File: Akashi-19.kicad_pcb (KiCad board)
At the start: 2 copper layers, 121.9 x 95.2 mm, 7 parts, among them J1 GROVE I2C, J2 Conn_01x20_Socket, J3 Conn_01x20_Socket, J4 QWIIC, J5 SERIAL, SW1 RESET, U1 Pico

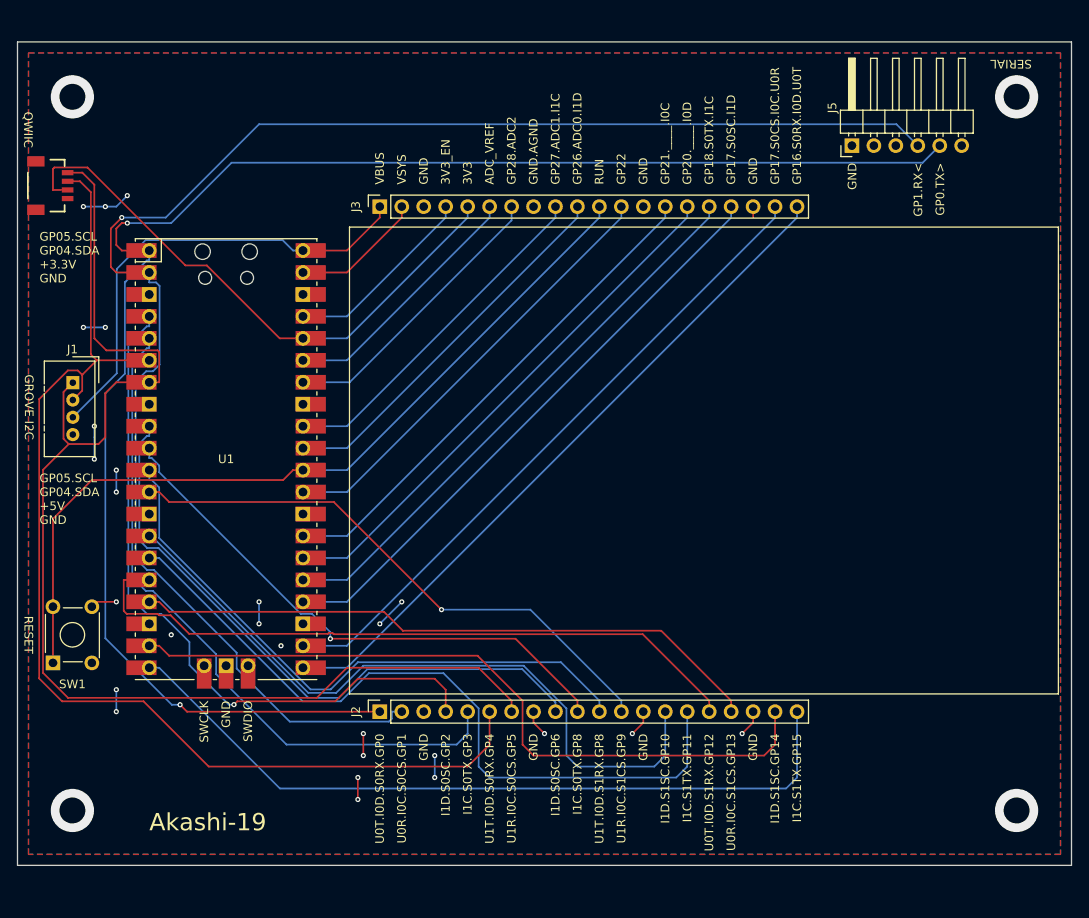
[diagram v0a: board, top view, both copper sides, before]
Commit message: Part position updated.
Wire is more beautiful.
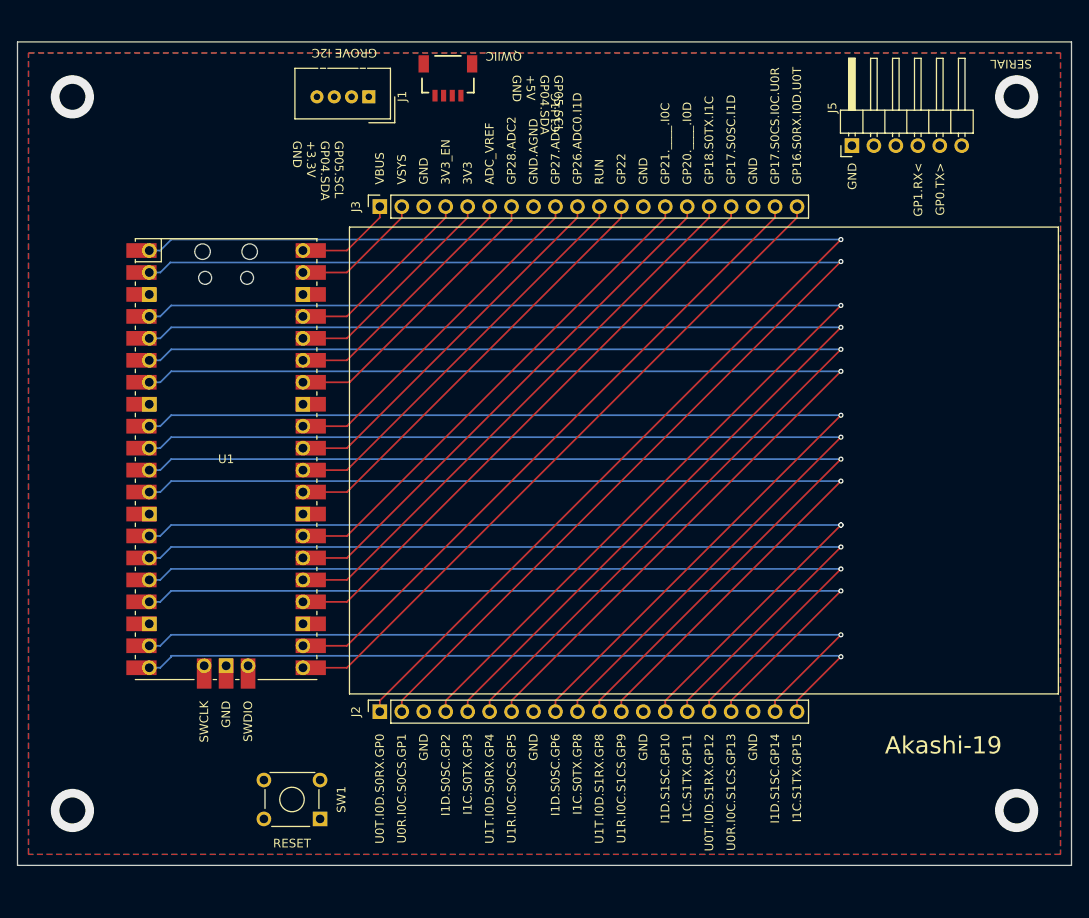
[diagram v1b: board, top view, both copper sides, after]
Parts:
- moved J1 47.6 mm to (128.3, 58.4), turned to -90 degrees
- moved J4 45.2 mm to (137.4, 58.3), turned to 180 degrees
- moved SW1 35.8 mm to (122.6, 141.9), turned to 180 degrees
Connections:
- J4 pad NC1: unconnected-(J4-NC-PadNC1) -> GND
- J4 pad NC2: unconnected-(J4-NC-PadNC2) -> GND
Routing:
- net Net-(J2-Pin_4): track 81.3 -> 146.5 mm
- net Net-(J2-Pin_5): track 79.9 -> 142.9 mm, vias 0 -> 1
- net Net-(J2-Pin_10): track 64.5 -> 124.9 mm
- net Net-(J2-Pin_9): track 73.6 -> 128.5 mm, vias 0 -> 1
- net Net-(J2-Pin_12): track 65.9 -> 117.7 mm
- net Net-(J2-Pin_11): track 71.1 -> 121.3 mm, vias 0 -> 1
- net Net-(J3-Pin_11): track 95.6 -> 47.7 mm
- net GND: track 44.3 -> 0.00 mm, vias 31 -> 4
- net +5V: track 54.4 -> 11.7 mm
- net +3.3V: track 66.7 -> 26.1 mm
- net /RX: track 184.8 -> 153.6 mm
- net /TX: track 187.7 -> 157.2 mm, vias 2 -> 1
- net Net-(J2-Pin_14): track 82.1 -> 110.5 mm, vias 0 -> 2
- net Net-(J2-Pin_17): track 73.3 -> 99.8 mm, vias 0 -> 1
- net Net-(J2-Pin_16): track 79.9 -> 103.4 mm, vias 0 -> 1
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
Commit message: Board resized.
111.7mm length.
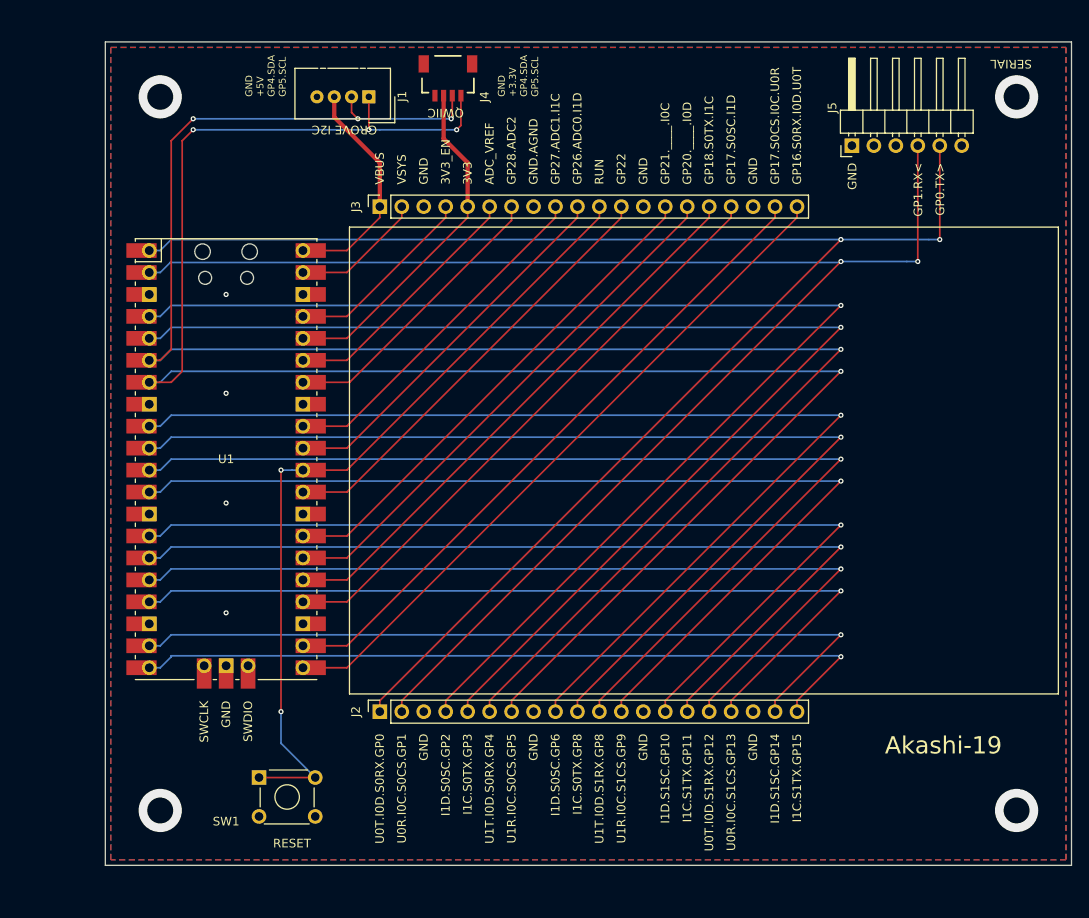
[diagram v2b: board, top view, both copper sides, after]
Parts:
- moved SW1 8.53 mm to (115.6, 137.2), turned to 0 degrees
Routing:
- net /SCL: track 135.7 -> 206.9 mm, vias 1 -> 4
- net /SDA: track 139.3 -> 205.4 mm, vias 1 -> 4
- net Net-(J3-Pin_11): track 47.7 -> 93.9 mm, vias 0 -> 2
- net /TX: track 157.2 -> 179.5 mm, vias 1 -> 2
- net /RX: track 153.6 -> 175.9 mm, vias 1 -> 2
- net +5V: track 11.7 -> 26.6 mm
- net +3.3V: track 26.1 -> 40.1 mm
- net Net-(J2-Pin_14): vias 2 -> 1
- net GND: vias 4 -> 8
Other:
- board size 121.9 x 95.2 mm -> 111.8 x 95.2 mm
- board text added: "GND +3.3V GP4.SDA GP5.SCL"
- board text added: "GND +5V GP4.SDA GP5.SCL"
- board text removed: "GP05.SCL GP04.SDA +3.3V GND"
- board text removed: "GP05.SCL GP04.SDA +5V GND"

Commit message: Change pin names font to NOTO SANS MONO
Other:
- board text added: "GND 3V3 GP4.SDA GP5.SCL"
- board text added: "GND VBUS GP4.SDA GP5.SCL"
- board text added: "U0T I0D S0RX GP0"
- board text removed: "GND +3.3V GP4.SDA GP5.SCL"
- board text removed: "GND +5V GP4.SDA GP5.SCL"
- board text removed: "U0T.I0D.S0RX.GP0"

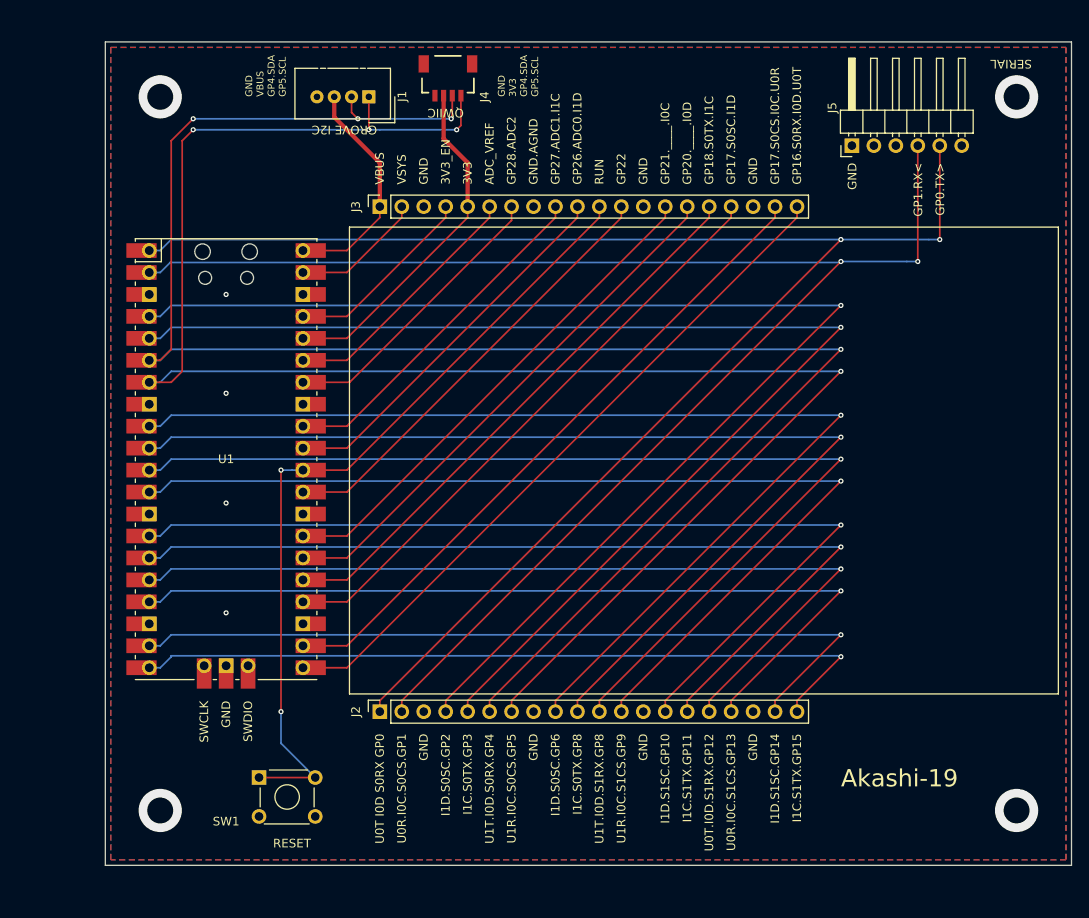
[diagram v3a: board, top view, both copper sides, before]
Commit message: Pin name description is updated.
- Separated by ' '.
- Grove and Qwiik description by table.
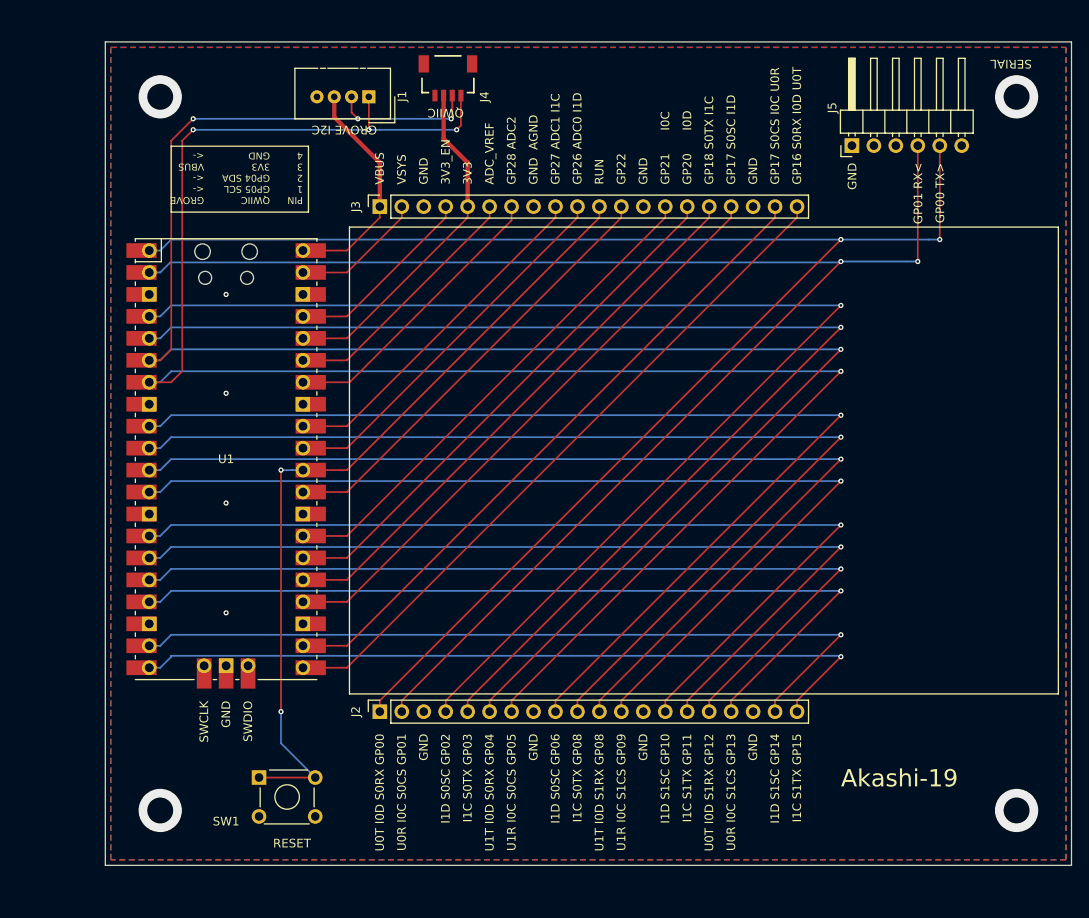
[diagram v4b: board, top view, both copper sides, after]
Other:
- board text added: "GND AGND"
- board text added: "GP00 TX>"
- board text added: "GP01 RX<"
- board text added: "GP16 S0RX I0D U0T"
- board text added: "GP17 S0CS I0C U0R"
- board text added: "GP17 S0SC I1D"
- board text added: "GP18 S0TX I1C"
- board text added: "GP20 I0D"
- board text added: "GP21 I0C"
- board text added: "GP26 ADC0 I1D"
- board text added: "GP27 ADC1 I1C"
- board text added: "GP28 ADC2"
- board text added: "GROVE <- <- VBUS <-"
- board text added: "I1C S0TX GP03"
- board text added: "I1C S0TX GP08"
- board text added: "I1C S1TX GP11"
- board text added: "I1C S1TX GP15"
- board text added: "I1D S0SC GP02"
- board text added: "I1D S0SC GP06"
- board text added: "I1D S1SC GP10"
- board text added: "I1D S1SC GP14"
- board text added: "PIN 1 2 3 4"
- board text added: "QWIIC GP05 SCL GP04 SDA 3V3 GND"
- board text added: "U0R I0C S0CS GP01"
- board text added: "U0R I0C S1CS GP13"
- board text added: "U0T I0D S0RX GP00"
- board text added: "U0T I0D S1RX GP12"
- board text added: "U1R I0C S0CS GP05"
- board text added: "U1R I0C S1CS GP09"
- board text added: "U1T I0D S0RX GP04"
- board text added: "U1T I0D S1RX GP08"
- board text removed: "GND 3V3 GP4.SDA GP5.SCL"
- board text removed: "GND VBUS GP4.SDA GP5.SCL"
- board text removed: "GND.AGND"
- board text removed: "GP0.TX>"
- board text removed: "GP1.RX<"
- board text removed: "GP16.S0RX.I0D.U0T"
- board text removed: "GP17.S0CS.I0C.U0R"
- board text removed: "GP17.S0SC.I1D"
- board text removed: "GP18.S0TX.I1C"
- board text removed: "GP20.____.I0D"
- board text removed: "GP21.____.I0C"
- board text removed: "GP26.ADC0.I1D"
- board text removed: "GP27.ADC1.I1C"
- board text removed: "GP28.ADC2"
- board text removed: "I1C.S0TX.GP3"
- board text removed: "I1C.S0TX.GP8"
- board text removed: "I1C.S1TX.GP11"
- board text removed: "I1C.S1TX.GP15"
- board text removed: "I1D.S0SC.GP2"
- board text removed: "I1D.S0SC.GP6"
- board text removed: "I1D.S1SC.GP10"
- board text removed: "I1D.S1SC.GP14"
- board text removed: "U0R.I0C.S0CS.GP1"
- board text removed: "U0R.I0C.S1CS.GP13"
- board text removed: "U0T I0D S0RX GP0"
- board text removed: "U0T.I0D.S1RX.GP12"
- board text removed: "U1R.I0C.S0CS.GP5"
- board text removed: "U1R.I0C.S1CS.GP9"
- board text removed: "U1T.I0D.S0RX.GP4"
- board text removed: "U1T.I0D.S1RX.GP8"

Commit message: The font of Signal name has been changed.
Now, Ubuntu Mono. 1.1mm
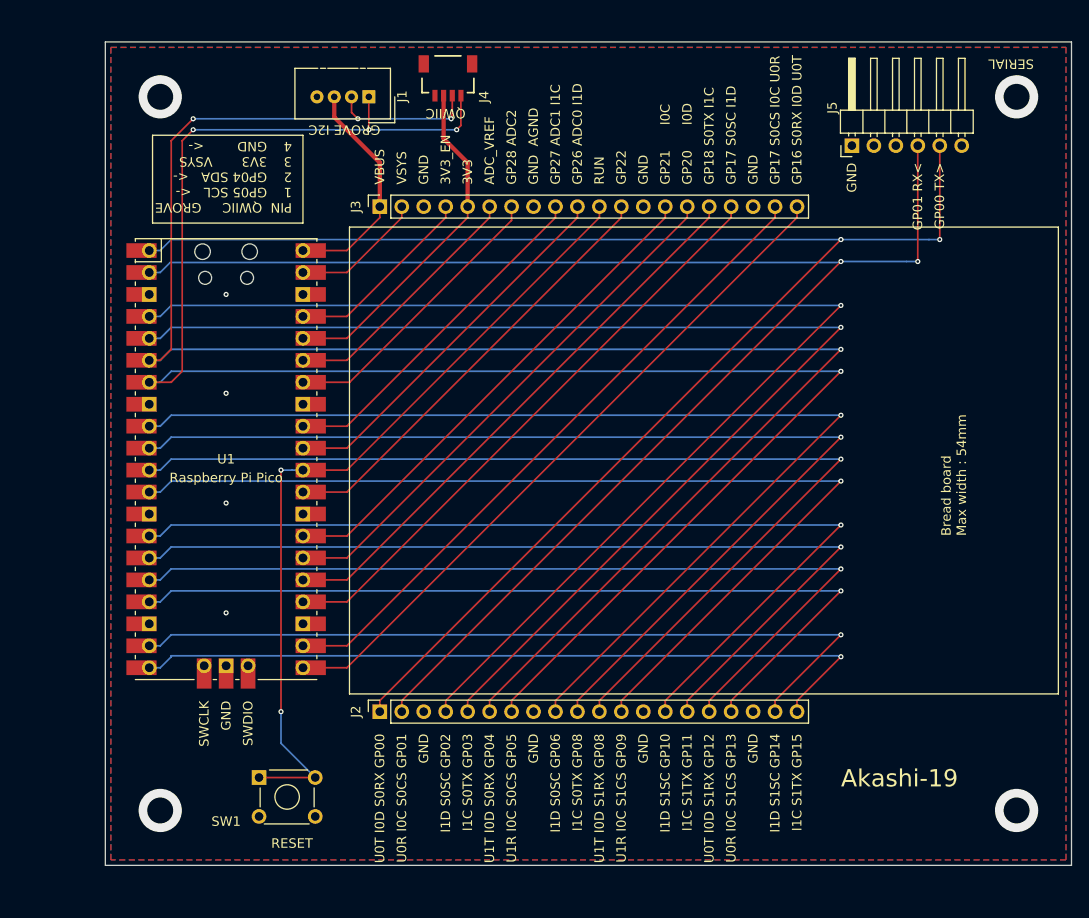
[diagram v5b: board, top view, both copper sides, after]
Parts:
- U1: value Pico -> Raspberry Pi Pico
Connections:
- J4 pad NC1: GND -> unconnected-(J4-NC-PadNC1)
- J4 pad NC2: GND -> unconnected-(J4-NC-PadNC2)
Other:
- board text added: "Bread board Max width : 54mm"
- board text added: "PIN QWIIC GROVE 1 GP05 SCL <- 2 GP04 SDA <- 3 3V3 VSYS 4 GND <-"
- board text removed: "GROVE <- <- VBUS <-"
- board text removed: "PIN 1 2 3 4"
- board text removed: "QWIIC GP05 SCL GP04 SDA 3V3 GND"

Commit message: Fix the text.
VSYS -> VBUS.
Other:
- board text added: "PIN QWIIC GROVE 1 GP05 SCL <- 2 GP04 SDA <- 3 3V3 VBUS 4 GND <-"
- board text removed: "PIN QWIIC GROVE 1 GP05 SCL <- 2 GP04 SDA <- 3 3V3 VSYS 4 GND <-"
